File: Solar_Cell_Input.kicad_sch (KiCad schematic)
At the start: 33 parts, among them Q201 NMOS, Q202 NMOS, Q203 NMOS, Q204 NMOS, U201 TMCS1101A2UQDT, U202 BQ24650

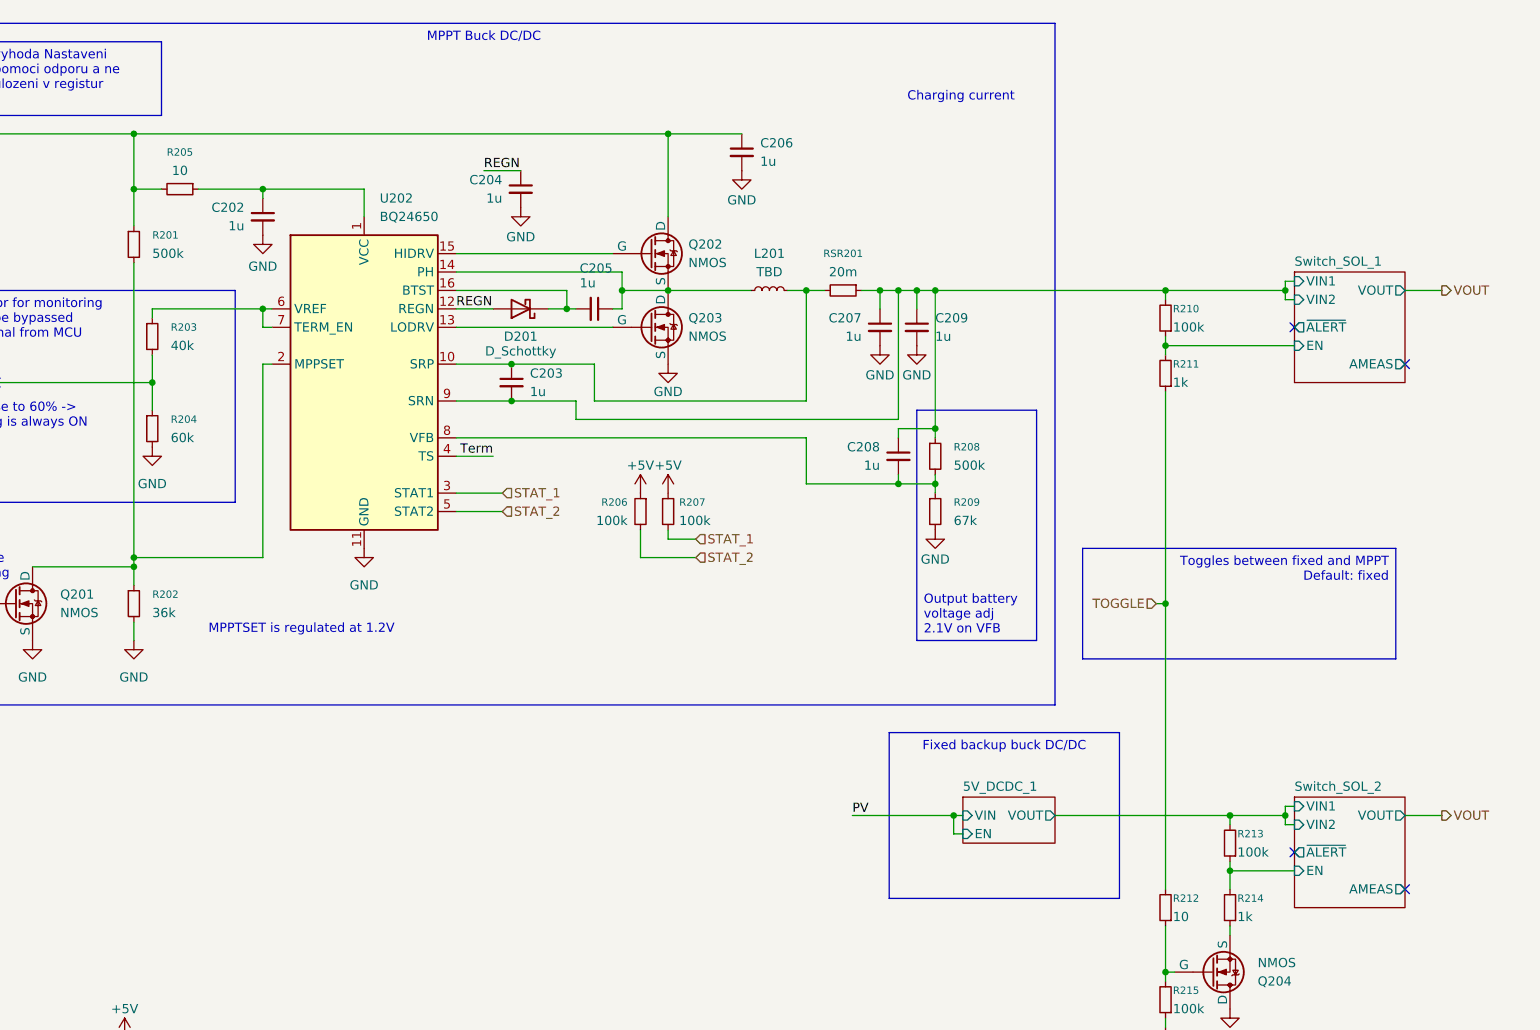
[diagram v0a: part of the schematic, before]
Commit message: deleted unused sheets, added standalone current measure sheet
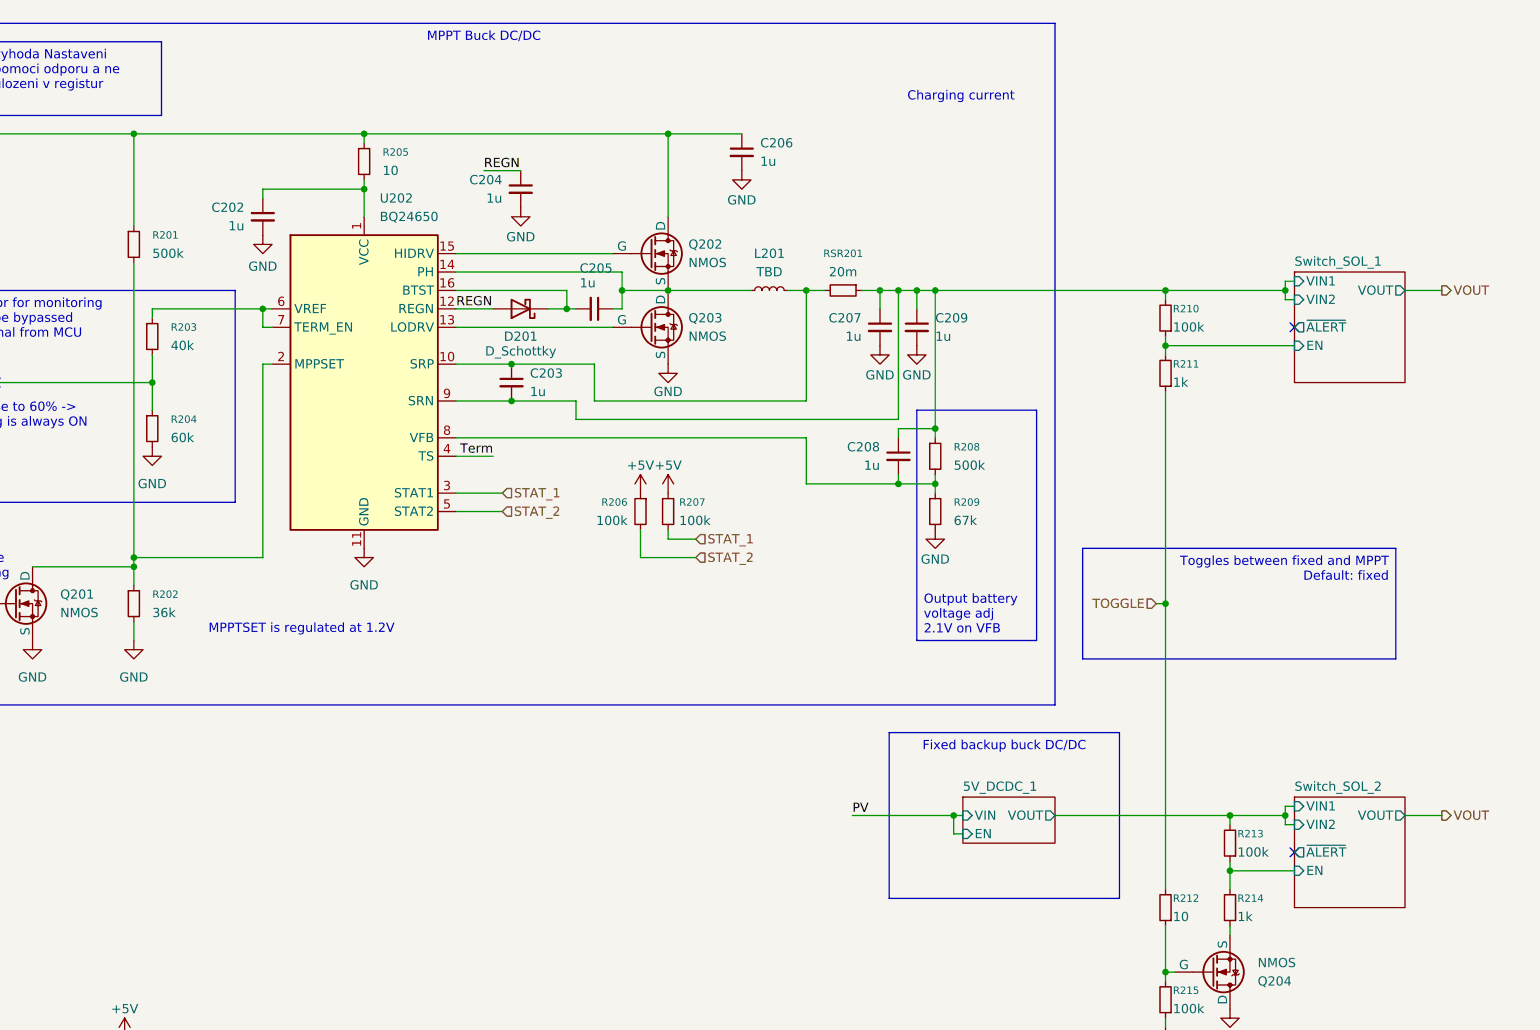
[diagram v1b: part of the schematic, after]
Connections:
- net PV: now also R205.1; no longer R205.2
- net at C202.1, U202.1 (VCC): now also R205.2; no longer R205.1
- no-connect marks 6 -> 4
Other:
- sheet Switch_SOL_1 ports: added none; removed AMEAS
- sheet Switch_SOL_2 ports: added none; removed AMEAS
- moved on the sheet: R205
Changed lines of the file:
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@@
 	)
 	(junction
-		(at 96.52 43.18)
-		(diameter 0)
-		(color 0 0 0 0)
-	)
-	(junction
 		(at 96.52 95.25)
 		(diameter 0)
@@
 	)
 	(junction
-		(at 207.01 57.15)
+		(at 128.27 43.18)
 		(diameter 0)
 		(color 0 0 0 0)
 	)
 	(junction
-		(at 114.3 43.18)
+		(at 207.01 57.15)
 		(diameter 0)
 		(color 0 0 0 0)
@@
 	)
 	(junction
+		(at 128.27 35.56)
+		(diameter 0)
+		(color 0 0 0 0)
+	)
+	(junction
 		(at 201.93 57.15)
 		(diameter 0)
@@
 	)
 	(no_connect
-		(at 271.78 67.31)
-	)
-	(no_connect
 		(at 256.54 134.62)
 	)
@@
 	)
 	(no_connect
-		(at 271.78 139.7)
-	)
-	(no_connect
 		(at 77.47 69.85)
 	)
@@
 	(wire
 		(pts
-			(xy 96.52 35.56) (xy 170.18 35.56)
+			(xy 96.52 35.56) (xy 128.27 35.56)
 		)
 		(stroke
@@
 	(wire
 		(pts
+			(xy 128.27 36.83) (xy 128.27 35.56)
+		)
+		(stroke
+			(width 0)
+			(type default)
+		)
+	)
+	(wire
+		(pts
 			(xy 144.78 40.64) (xy 149.86 40.64)
 		)
@@
 	(wire
 		(pts
-			(xy 96.52 35.56) (xy 96.52 43.18)
+			(xy 96.52 35.56) (xy 96.52 48.26)
 		)
 		(stroke
@@
 	(wire
 		(pts
-			(xy 96.52 43.18) (xy 100.33 43.18)
-		)
-		(stroke
-			(width 0)
-			(type default)
-		)
-	)
-	(wire
-		(pts
 			(xy 247.65 139.7) (xy 247.65 137.16)
 		)
@@
 	(wire
 		(pts
-			(xy 160.02 72.39) (xy 189.23 72.39)
+			(xy 128.27 41.91) (xy 128.27 43.18)
 		)
 		(stroke
@@
 	(wire
 		(pts
-			(xy 140.97 87.63) (xy 147.32 87.63)
+			(xy 160.02 72.39) (xy 189.23 72.39)
 		)
 		(stroke
@@
 	(wire
 		(pts
-			(xy 238.76 152.4) (xy 238.76 151.13)
+			(xy 140.97 87.63) (xy 147.32 87.63)
 		)
 		(stroke
@@
 	(wire
 		(pts
-			(xy 238.76 58.42) (xy 238.76 57.15)
+			(xy 238.76 152.4) (xy 238.76 151.13)
 		)
 		(stroke
@@
 	(wire
 		(pts
-			(xy 96.52 43.18) (xy 96.52 48.26)
+			(xy 238.76 58.42) (xy 238.76 57.15)
 		)
 		(stroke
@@
 	(wire
 		(pts
-			(xy 140.97 62.23) (xy 162.56 62.23)
+			(xy 128.27 35.56) (xy 170.18 35.56)
 		)
 		(stroke
@@
 	(wire
 		(pts
-			(xy 156.21 57.15) (xy 140.97 57.15)
+			(xy 140.97 62.23) (xy 162.56 62.23)
 		)
 		(stroke
@@
 	(wire
 		(pts
-			(xy 96.52 53.34) (xy 96.52 93.98)
+			(xy 156.21 57.15) (xy 140.97 57.15)
 		)
 		(stroke
@@
 	(wire
 		(pts
-			(xy 207.01 76.2) (xy 207.01 77.47)
+			(xy 96.52 53.34) (xy 96.52 93.98)
 		)
 		(stroke
@@
 	(wire
 		(pts
-			(xy 238.76 100.33) (xy 238.76 139.7)
+			(xy 207.01 76.2) (xy 207.01 77.47)
 		)
 		(stroke
@@
 	(wire
 		(pts
-			(xy 114.3 93.98) (xy 114.3 67.31)
+			(xy 238.76 100.33) (xy 238.76 139.7)
 		)
 		(stroke
@@
 	(wire
 		(pts
-			(xy 74.93 181.61) (xy 85.09 181.61)
+			(xy 114.3 93.98) (xy 114.3 67.31)
 		)
 		(stroke
@@
 	(wire
 		(pts
-			(xy 105.41 43.18) (xy 114.3 43.18)
+			(xy 74.93 181.61) (xy 85.09 181.61)
 		)
 		(stroke
@@
 	(symbol
 		(lib_id "Device:R_Small")
-		(at 102.87 43.18 270)
+		(at 128.27 39.37 0)
 		(unit 1)
 		(exclude_from_sim no)
@@
 		(fields_autoplaced yes)
 		(property "Reference" "R205"
-			(at 102.87 38.1 90)
+			(at 130.81 38.0999 0)
 			(effects
 				(font
 					(size 1.016 1.016)
 				)
+				(justify left)
 			)
 		)
 		(property "Value" "10"
-			(at 102.87 40.64 90)
+			(at 130.81 40.6399 0)
 			(effects
 				(font
 					(size 1.27 1.27)
 				)
+				(justify left)
 			)
 		)
 		(property "Footprint" "Resistor_SMD:R_0603_1608Metric_Pad0.98x0.95mm_HandSolder"
-			(at 102.87 43.18 0)
+			(at 128.27 39.37 0)
 			(effects
 				(font
@@
 		)
 		(property "Datasheet" "~"
-			(at 102.87 43.18 0)
+			(at 128.27 39.37 0)
 			(effects
 				(font
@@
 		)
 		(property "Description" "Resistor, small symbol"
-			(at 102.87 43.18 0)
+			(at 128.27 39.37 0)
 			(effects
 				(font
@@
 			(project "EPS"
 				(path "/94201994-47b8-4213-8d1a-05da12b2a7b0/4e89c933-7889-465d-8e1a-713a5947b2aa"
-					(reference "R3105")
+					(reference "R205")
 					(unit 1)
 				)
 				(path "/94201994-47b8-4213-8d1a-05da12b2a7b0/80284205-18d0-4824-96a2-1f6126c1d232"
-					(reference "R405")
+					(reference "R205")
 					(unit 1)
 				)
@@
 				)
 				(path "/94201994-47b8-4213-8d1a-05da12b2a7b0/b1cfc9a6-bdf2-4ebb-ae2c-6da62e7f592e"
-					(reference "R305")
+					(reference "R205")
 					(unit 1)
 				)
 				(path "/94201994-47b8-4213-8d1a-05da12b2a7b0/cfc4b703-44df-4518-ae41-36cc43a226e9"
-					(reference "R6205")
+					(reference "R205")
 					(unit 1)
 				)
 				(path "/94201994-47b8-4213-8d1a-05da12b2a7b0/d31c76f0-06ec-4dd4-b64f-0900d628aaef"
-					(reference "R8205")
+					(reference "R205")
 					(unit 1)
 				)
@@
 			)
 		)
-		(pin "AMEAS" output
-			(at 271.78 67.31 0)
-			(effects
-				(font
-					(size 1.27 1.27)
-				)
-				(justify right)
-			)
-		)
 		(pin "EN" input
 			(at 256.54 64.77 180)
@@
 			)
 		)
-		(pin "AMEAS" output
-			(at 271.78 139.7 0)
-			(effects
-				(font
-					(size 1.27 1.27)
-				)
-				(justify right)
-			)
-		)

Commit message: minor adjustments
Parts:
- removed C201: 1u, Capacitor_SMD:C_0603_1608Metric_Pad1.08x0.95mm_HandSolder, symbol Device:C_Small
- removed U201: TMCS1101A2UQDT, Package_SO:SOIC-8_3.9x4.9mm_P1.27mm, symbol Sensor_Current:ACS723xLCTR-40AB
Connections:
- no-connect marks 4 -> 3
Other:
- added sheet AMEAS_1 (Current_Measure.kicad_sch)

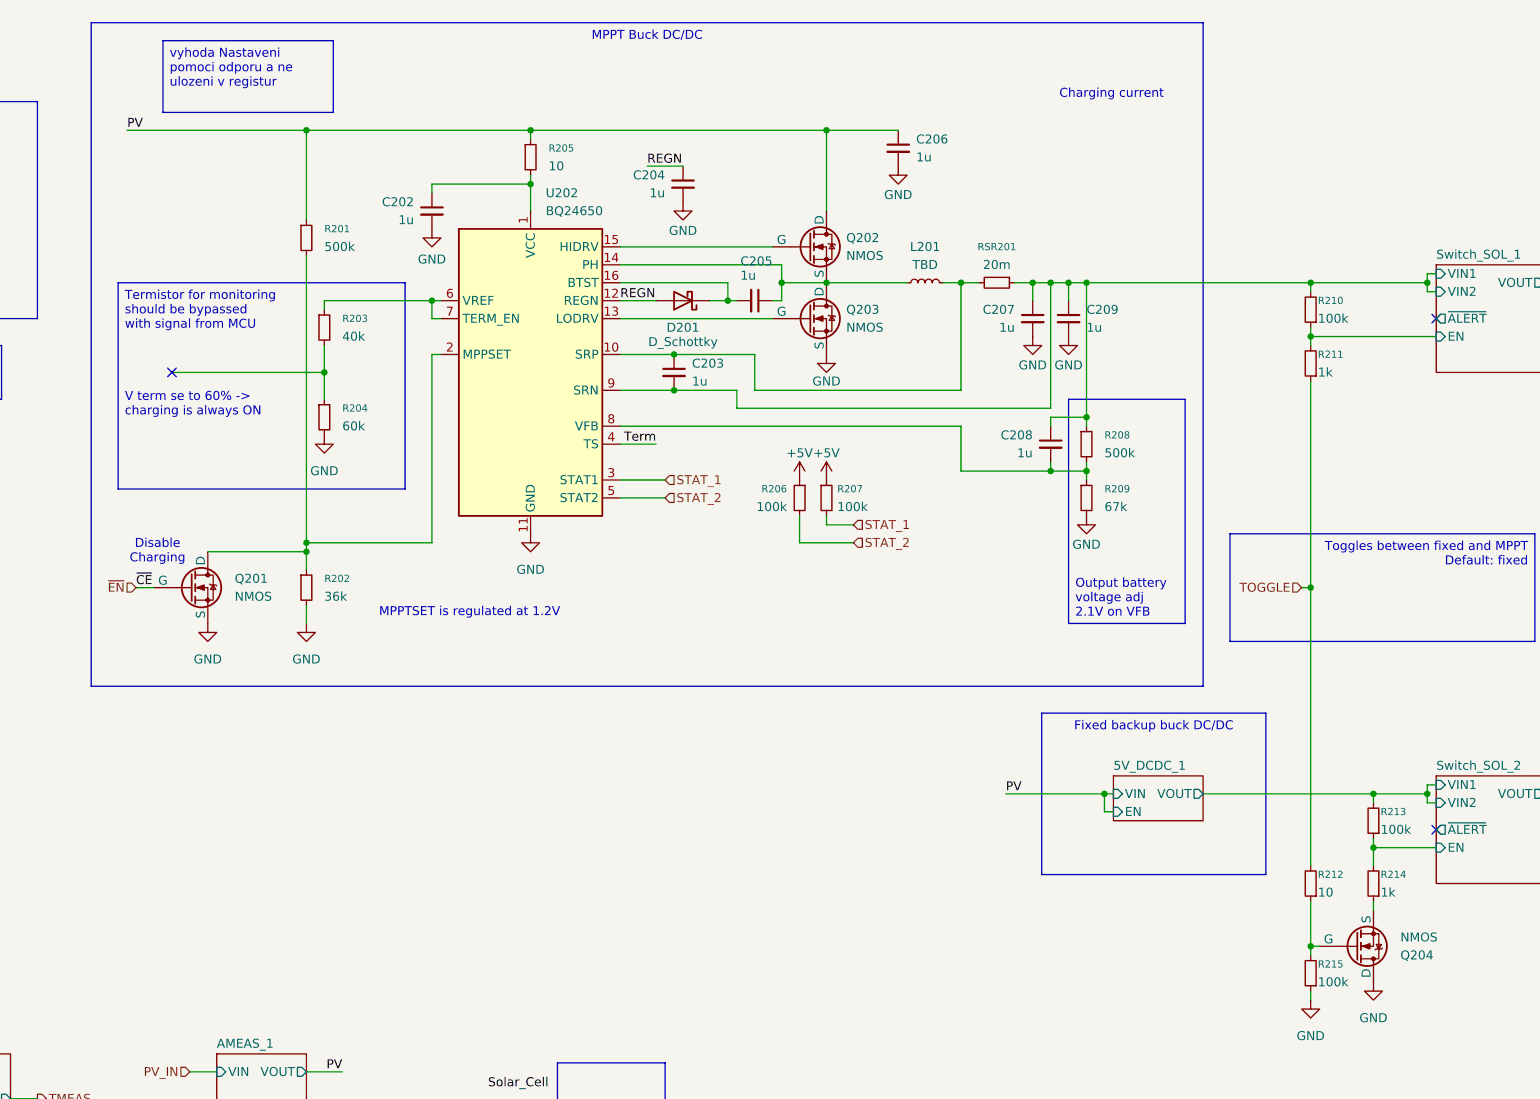
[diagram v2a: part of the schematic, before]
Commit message: wired channel alerts; added schematic for test pbc
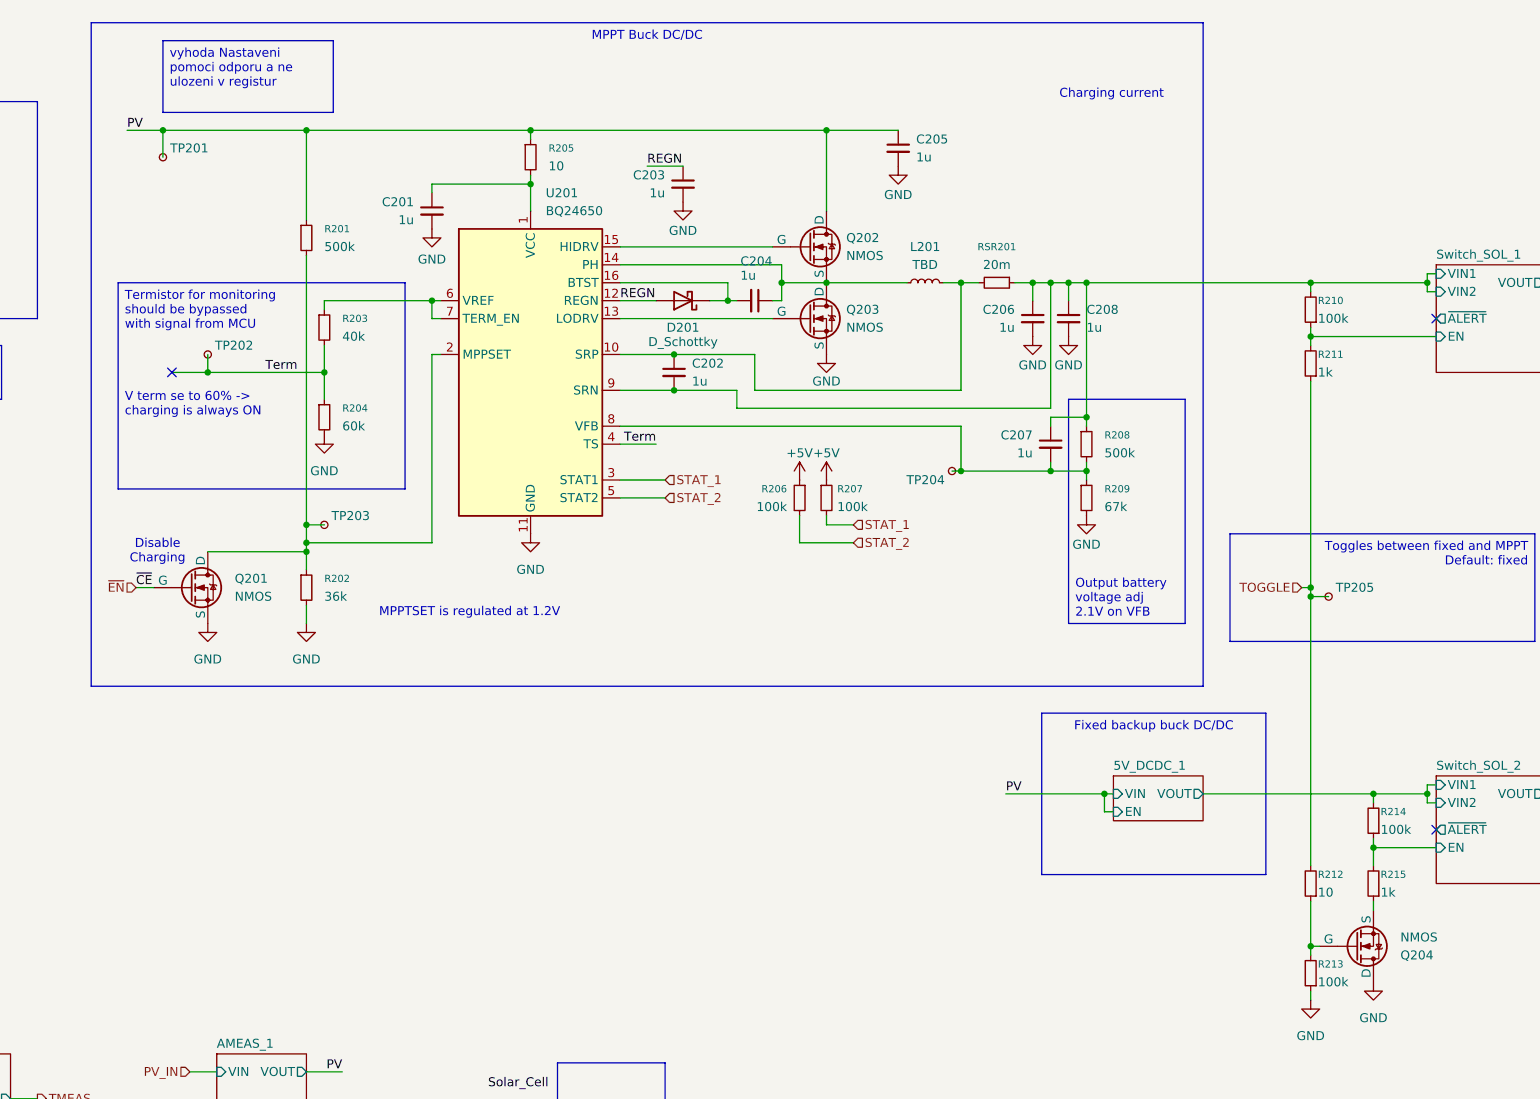
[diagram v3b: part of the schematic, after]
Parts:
- added TP201, TP202, TP203, TP204, TP205: ~, TestPoint:TestPoint_Pad_1.0x1.0mm, symbol Connector:TestPoint_Small
- renumbered C202 to C201, C203 to C202, C204 to C203, C205 to C204, C206 to C205, C207 to C206, C208 to C207, C209 to C208, R215 to R213, R213 to R214, R214 to R215, U202 to U201
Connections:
- net PV: now also TP201.1
- net TOGGLE: now also TP205.1
- net Term: now also R203.2, R204.1, TP202.1
- net at C207.2, R208.2, R209.1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: now also TP204.1
- net at Q201.1 (D), R201.2, R202.1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: now also TP203.1
